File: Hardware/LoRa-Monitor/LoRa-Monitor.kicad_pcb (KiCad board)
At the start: 2 copper layers, 81 parts, among them Q1 ZXTN25100DFH, Q2 ZXTN25100DFH, Q3 ZXTN25100DFH, Q4 ZXTN25100DFH, Q5 ZXTN25100DFH, Q6 ZXTN25100DFH, U1 IRM-05-5, U10 ESP32-S3-WROOM-1, U2 ACPL-M61L, U3 ACPL-M61L, U4 ACPL-M61L, U5 ACPL-M61L, U6 ACPL-M61L, U7 ACPL-M61L, U8 MAX3483, U9 BQ24072RGT

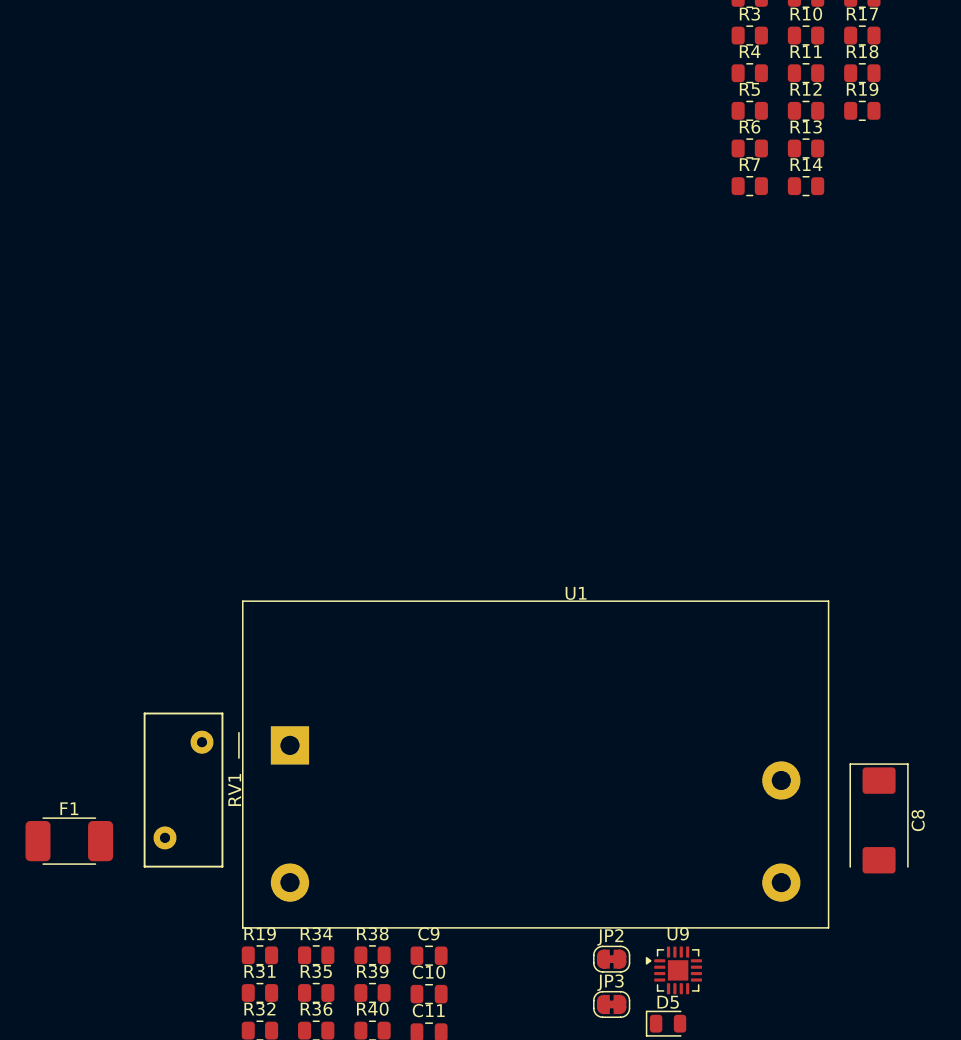
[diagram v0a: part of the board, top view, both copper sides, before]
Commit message: Added more PSU components.
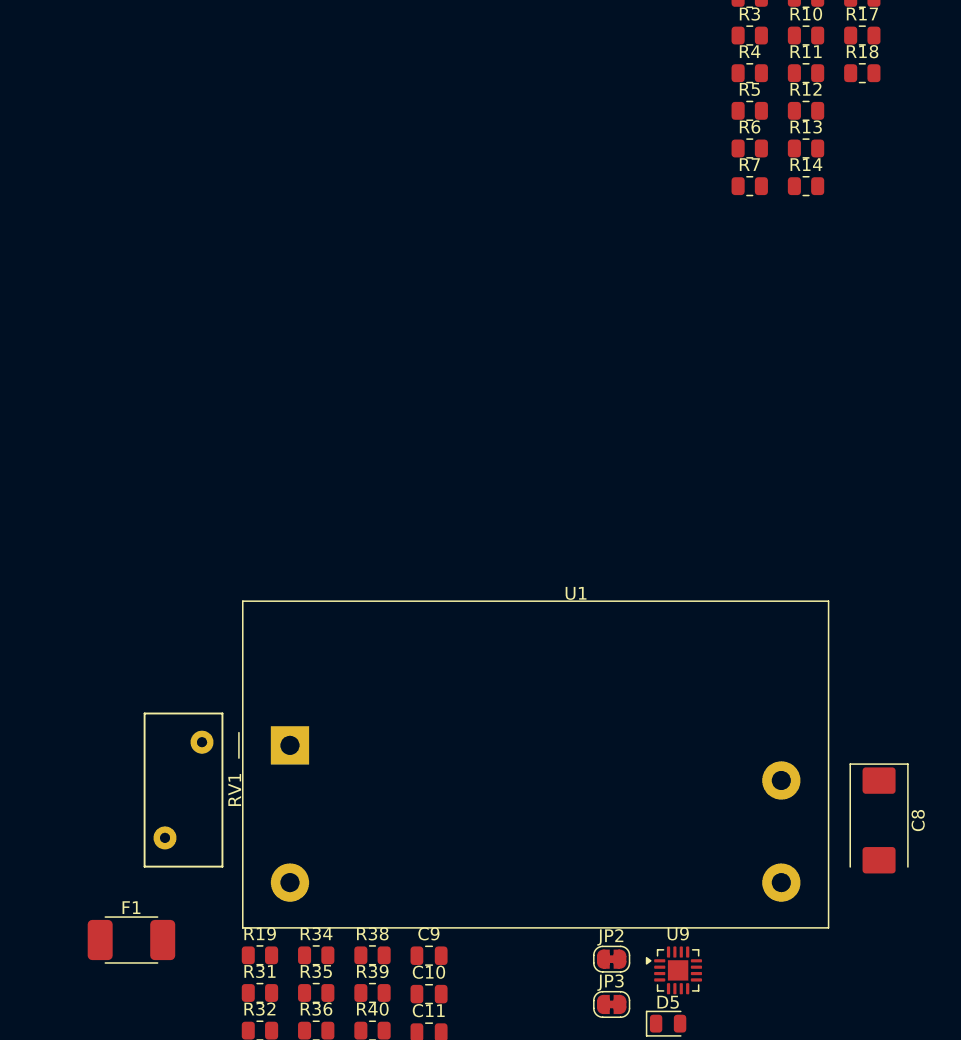
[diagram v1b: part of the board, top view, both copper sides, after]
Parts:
- removed the R19 at (117.7, 78.8)
- U1: footprint Converter_ACDC:Converter_ACDC_MeanWell_IRM-05-xx_THT -> DeviceComponents:Converter_ACDC_MeanWell_IRM-05-xx_THT
- U9: footprint Package_DFN_QFN:VQFN-16-1EP_3x3mm_P0.5mm_EP1.6x1.6mm -> DeviceComponents:VQFN-16-1EP_3x3mm_P0.5mm_EP1.6x1.6mm
- moved F1 9.15 mm to (60.2, 143.8)

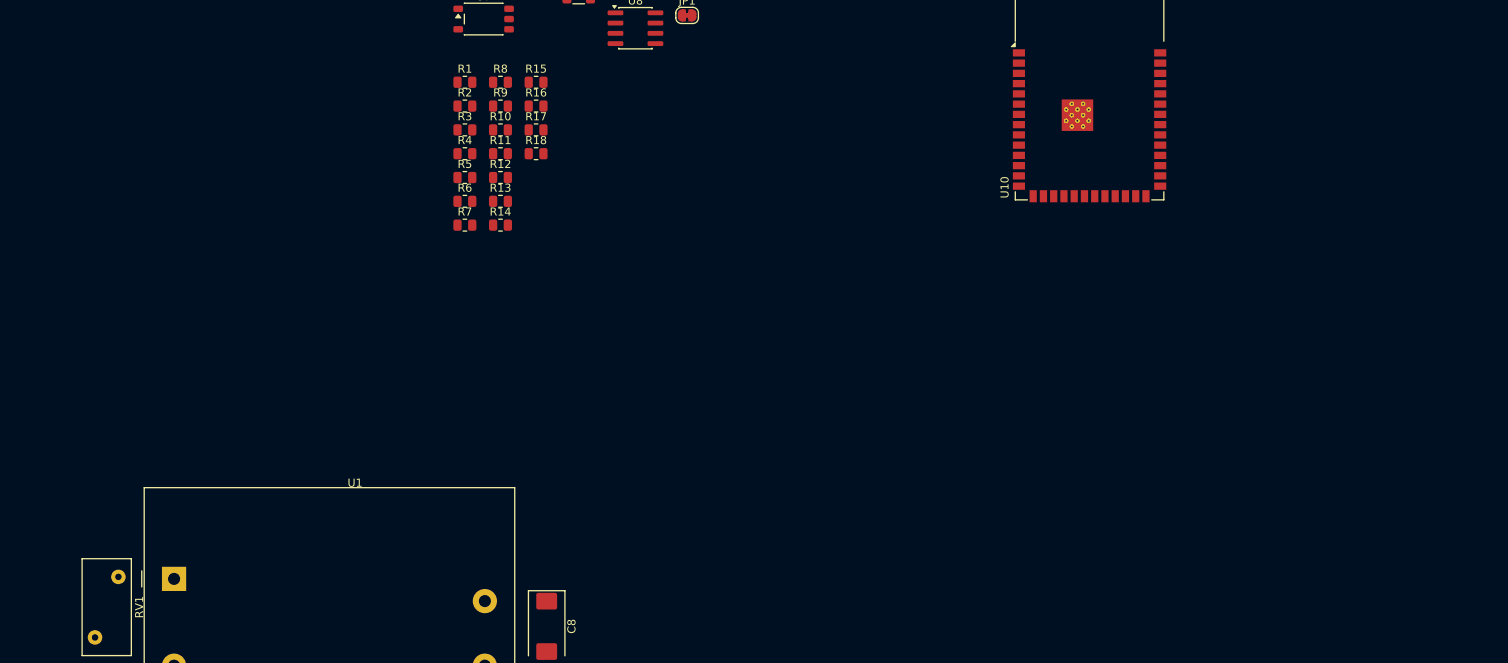
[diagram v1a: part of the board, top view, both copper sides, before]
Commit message: Finished PSU module, started Energy meter
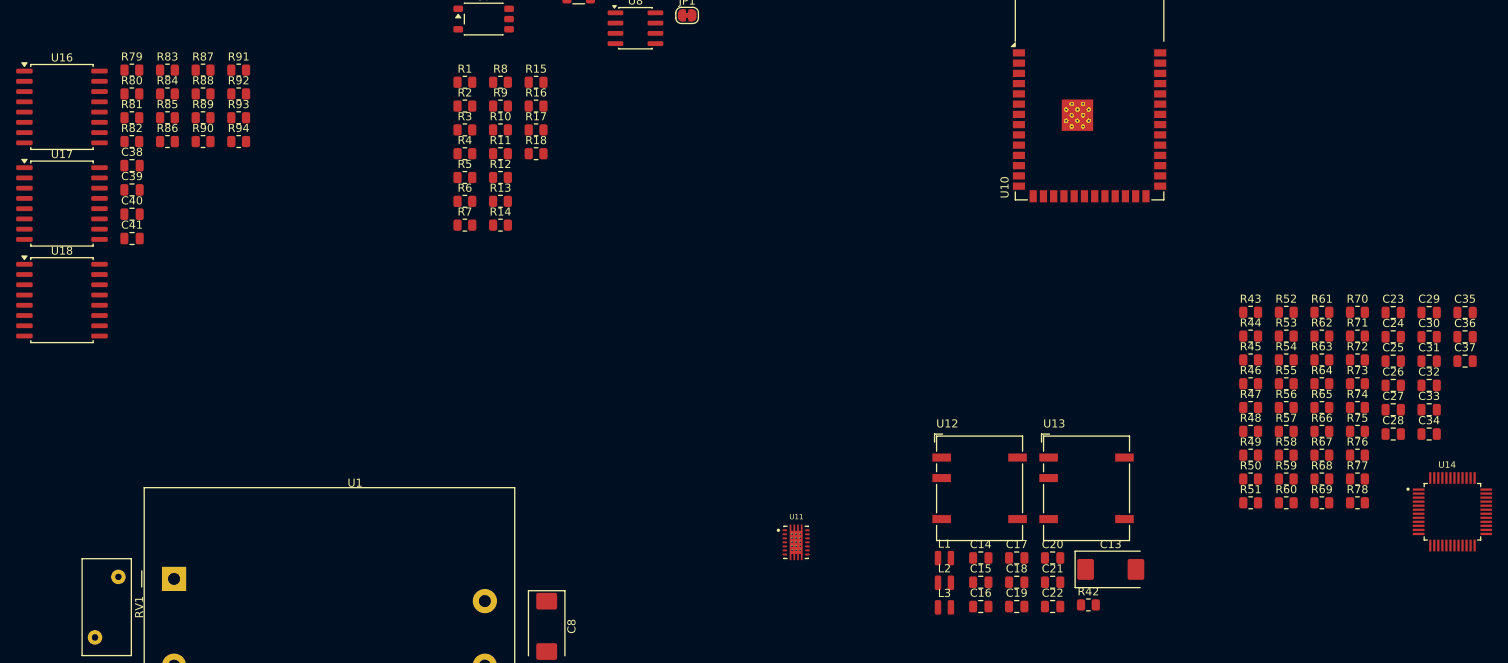
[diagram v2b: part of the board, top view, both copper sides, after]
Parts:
- added C13: 100uF 16V, Capacitor_Tantalum_SMD:CP_EIA-7343-31_Kemet-D, F.Cu at (188.9, 127.3)
- added C14: 10uF, Capacitor_SMD:C_0805_2012Metric, F.Cu at (172.8, 125.9)
- added C15: 10uF, Capacitor_SMD:C_0805_2012Metric, F.Cu at (172.8, 128.9)
- added C16: 22uF, Capacitor_SMD:C_0805_2012Metric, F.Cu at (172.8, 131.9)
- added C17: 100nF, Capacitor_SMD:C_0805_2012Metric, F.Cu at (177.2, 125.9)
- added C18: 1uF, Capacitor_SMD:C_0805_2012Metric, F.Cu at (177.2, 128.9)
- added C19: 22uF, Capacitor_SMD:C_0805_2012Metric, F.Cu at (177.2, 131.9)
- added C20: 22uF, Capacitor_SMD:C_0805_2012Metric, F.Cu at (181.7, 125.9)
- added C21: 100nF, Capacitor_SMD:C_0805_2012Metric, F.Cu at (181.7, 128.9)
- added C22: 1uF, Capacitor_SMD:C_0805_2012Metric, F.Cu at (181.7, 131.9)
- added C23: 4.7uF, Capacitor_SMD:C_0805_2012Metric, F.Cu at (223.9, 95.5)
- added C24: 100nF, Capacitor_SMD:C_0805_2012Metric, F.Cu at (223.9, 98.5)
- added C25: 10uF, Capacitor_SMD:C_0805_2012Metric, F.Cu at (223.9, 101.5)
- added C26: 100nF, Capacitor_SMD:C_0805_2012Metric, F.Cu at (223.9, 104.5)
- added C27: 100nF, Capacitor_SMD:C_0805_2012Metric, F.Cu at (223.9, 107.5)
- added C28: 100nF, Capacitor_SMD:C_0805_2012Metric, F.Cu at (223.9, 110.6)
- added C29: 100nF, Capacitor_SMD:C_0805_2012Metric, F.Cu at (228.3, 95.5)
- added C30: 18nF, Capacitor_SMD:C_0805_2012Metric, F.Cu at (228.3, 98.5)
- added C31: 18nf, Capacitor_SMD:C_0805_2012Metric, F.Cu at (228.3, 101.5)
- added C32: 18nF, Capacitor_SMD:C_0805_2012Metric, F.Cu at (228.3, 104.5)
- added C33: 18nf, Capacitor_SMD:C_0805_2012Metric, F.Cu at (228.3, 107.5)
- added C34: 18nF, Capacitor_SMD:C_0805_2012Metric, F.Cu at (228.3, 110.6)
- added C35: 18nf, Capacitor_SMD:C_0805_2012Metric, F.Cu at (232.8, 95.5)
- added C36: 18nF, Capacitor_SMD:C_0805_2012Metric, F.Cu at (232.8, 98.5)
- added C37: 18nF, Capacitor_SMD:C_0805_2012Metric, F.Cu at (232.8, 101.5)
- added C38: 18nF, Capacitor_SMD:C_0805_2012Metric, F.Cu at (67.6, 77.3)
- added C39: 18nF, Capacitor_SMD:C_0805_2012Metric, F.Cu at (67.6, 80.3)
- added C40: 18nF, Capacitor_SMD:C_0805_2012Metric, F.Cu at (67.6, 83.3)
- added C41: 18nF, Capacitor_SMD:C_0805_2012Metric, F.Cu at (67.6, 86.3)
- added L1: 1uH, DeviceComponents:L_0806_2016Metric, F.Cu at (168.3, 125.9)
- added L2: 15uH, DeviceComponents:L_0806_2016Metric, F.Cu at (168.3, 129.0)
- added L3: 15uH, DeviceComponents:L_0806_2016Metric, F.Cu at (168.3, 132.0)
- added R42: 10k, Resistor_SMD:R_0805_2012Metric, F.Cu at (186.1, 131.7)
- added R43: 10k, Resistor_SMD:R_0805_2012Metric, F.Cu at (206.2, 95.5)
- added R44: 10k, Resistor_SMD:R_0805_2012Metric, F.Cu at (206.2, 98.4)
- added R45: 10k, Resistor_SMD:R_0805_2012Metric, F.Cu at (206.2, 101.4)
- added R46: 10k, Resistor_SMD:R_0805_2012Metric, F.Cu at (206.2, 104.3)
- added R47: 10k, Resistor_SMD:R_0805_2012Metric, F.Cu at (206.2, 107.3)
- added R48: 240k, Resistor_SMD:R_0805_2012Metric, F.Cu at (206.2, 110.2)
- added R49: 240k, Resistor_SMD:R_0805_2012Metric, F.Cu at (206.2, 113.2)
- added R50: 240k, Resistor_SMD:R_0805_2012Metric, F.Cu at (206.2, 116.1)
- added R51: 240k, Resistor_SMD:R_0805_2012Metric, F.Cu at (206.2, 119.1)
- added R52: 240k, Resistor_SMD:R_0805_2012Metric, F.Cu at (210.6, 95.5)
- added R53: 240k, Resistor_SMD:R_0805_2012Metric, F.Cu at (210.6, 98.4)
- added R54: 240k, Resistor_SMD:R_0805_2012Metric, F.Cu at (210.6, 101.4)
- added R55: 1k, Resistor_SMD:R_0805_2012Metric, F.Cu at (210.6, 104.3)
- added R56: 1k, Resistor_SMD:R_0805_2012Metric, F.Cu at (210.6, 107.3)
- added R57: 240k, Resistor_SMD:R_0805_2012Metric, F.Cu at (210.6, 110.2)
- added R58: 240k, Resistor_SMD:R_0805_2012Metric, F.Cu at (210.6, 113.2)
- added R59: 240k, Resistor_SMD:R_0805_2012Metric, F.Cu at (210.6, 116.1)
- added R60: 240k, Resistor_SMD:R_0805_2012Metric, F.Cu at (210.6, 119.1)
- added R61: 240k, Resistor_SMD:R_0805_2012Metric, F.Cu at (215.0, 95.5)
- added R62: 240k, Resistor_SMD:R_0805_2012Metric, F.Cu at (215.0, 98.4)
- added R63: 240k, Resistor_SMD:R_0805_2012Metric, F.Cu at (215.0, 101.4)
- added R64: 1k, Resistor_SMD:R_0805_2012Metric, F.Cu at (215.0, 104.3)
- added R65: 1k, Resistor_SMD:R_0805_2012Metric, F.Cu at (215.0, 107.3)
- added R66: 240k, Resistor_SMD:R_0805_2012Metric, F.Cu at (215.0, 110.2)
- added R67: 240k, Resistor_SMD:R_0805_2012Metric, F.Cu at (215.0, 113.2)
- added R68: 240k, Resistor_SMD:R_0805_2012Metric, F.Cu at (215.0, 116.1)
- added R69: 240k, Resistor_SMD:R_0805_2012Metric, F.Cu at (215.0, 119.1)
- added R70: 240k, Resistor_SMD:R_0805_2012Metric, F.Cu at (219.4, 95.5)
- added R71: 240k, Resistor_SMD:R_0805_2012Metric, F.Cu at (219.4, 98.4)
- added R72: 240k, Resistor_SMD:R_0805_2012Metric, F.Cu at (219.4, 101.4)
- added R73: 1k, Resistor_SMD:R_0805_2012Metric, F.Cu at (219.4, 104.3)
- added R74: 1k, Resistor_SMD:R_0805_2012Metric, F.Cu at (219.4, 107.3)
- added R75: 2.4R, Resistor_SMD:R_0805_2012Metric, F.Cu at (219.4, 110.2)
- added R76: 2.4R, Resistor_SMD:R_0805_2012Metric, F.Cu at (219.4, 113.2)
- added R77: 1k, Resistor_SMD:R_0805_2012Metric, F.Cu at (219.4, 116.1)
- added R78: 1k, Resistor_SMD:R_0805_2012Metric, F.Cu at (219.4, 119.1)
- added R79: 2.4R, Resistor_SMD:R_0805_2012Metric, F.Cu at (67.6, 65.5)
- added R80: 2.4R, Resistor_SMD:R_0805_2012Metric, F.Cu at (67.6, 68.4)
- added R81: 1k, Resistor_SMD:R_0805_2012Metric, F.Cu at (67.6, 71.4)
- added R82: 1k, Resistor_SMD:R_0805_2012Metric, F.Cu at (67.6, 74.3)
- added R83: 2.4R, Resistor_SMD:R_0805_2012Metric, F.Cu at (72.0, 65.5)
- added R84: 2.4R, Resistor_SMD:R_0805_2012Metric, F.Cu at (72.0, 68.4)
- added R85: 1k, Resistor_SMD:R_0805_2012Metric, F.Cu at (72.0, 71.4)
- added R86: 1k, Resistor_SMD:R_0805_2012Metric, F.Cu at (72.0, 74.3)
- added R87: 10k, Resistor_SMD:R_0805_2012Metric, F.Cu at (76.4, 65.5)
- added R88: 10k, Resistor_SMD:R_0805_2012Metric, F.Cu at (76.4, 68.4)
- added R89: 10k, Resistor_SMD:R_0805_2012Metric, F.Cu at (76.4, 71.4)
- added R90: 10k, Resistor_SMD:R_0805_2012Metric, F.Cu at (76.4, 74.3)
- added R91: 10k, Resistor_SMD:R_0805_2012Metric, F.Cu at (80.8, 65.5)
- added R92: 10k, Resistor_SMD:R_0805_2012Metric, F.Cu at (80.8, 68.4)
- added R93: 10k, Resistor_SMD:R_0805_2012Metric, F.Cu at (80.8, 71.4)
- added R94: 10k, Resistor_SMD:R_0805_2012Metric, F.Cu at (80.8, 74.3)
- added U11: TPS63021DSJR, DeviceComponents:IC_TPS63021DSJR, F.Cu at (149.9, 124.0)
- added U12: NXE1S0303MC, Converter_DCDC:Converter_DCDC_Murata_NXExSxxxxMC_SMD, F.Cu at (172.6, 118.5)
- added U13: NXE1S0303MC, Converter_DCDC:Converter_DCDC_Murata_NXExSxxxxMC_SMD, F.Cu at (185.9, 118.5)
- added U14: ATM90E32AS-AU-R, DeviceComponents:QFP50P900X900X120-48N, F.Cu at (231.2, 120.2)
- added U16: ADuM1401xRW, Package_SO:SOIC-16W_7.5x10.3mm_P1.27mm, F.Cu at (59.0, 70.0)
- added U17: ADuM1401xRW, Package_SO:SOIC-16W_7.5x10.3mm_P1.27mm, F.Cu at (59.0, 82.0)
- added U18: ADuM1401xRW, Package_SO:SOIC-16W_7.5x10.3mm_P1.27mm, F.Cu at (59.0, 94.0)

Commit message: Finished schematic, started with PCB design
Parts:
- added C42: 100nF, Capacitor_SMD:C_0805_2012Metric, F.Cu at (282.9, 111.8)
- added C43: 100nF, Capacitor_SMD:C_0805_2012Metric, F.Cu at (378.7, 48.1)
- added C44: 10uF, Capacitor_SMD:C_0805_2012Metric, F.Cu at (378.7, 51.1)
- added C45: 100nF, Capacitor_SMD:C_0805_2012Metric, F.Cu at (351.1, 77.1)
- added C46: 10uF, Capacitor_SMD:C_0805_2012Metric, F.Cu at (263.1, -52.1)
- added C47: 100nF, Capacitor_SMD:C_0805_2012Metric, F.Cu at (265.3, -52.1)
- added C48: 10uF, Capacitor_SMD:C_0805_2012Metric, F.Cu at (282.9, 114.8)
- added C49: 100nF, Capacitor_SMD:C_0805_2012Metric, F.Cu at (282.9, 117.8)
- added C50: 10uF, Capacitor_SMD:C_0805_2012Metric, F.Cu at (282.9, 120.8)
- added C51: 10uF, Capacitor_SMD:C_0805_2012Metric, F.Cu at (282.9, 123.8)
- added D6: SK6812MINI-012, DeviceComponents:LED_SK6812MINI-012, F.Cu at (350.1, 81.8)
- added J1: USB_C_Receptacle_USB2.0_16P, Connector_USB:USB_C_Receptacle_HRO_TYPE-C-31-M-12, F.Cu at (247.1, -49.6)
- added J10: AudioJack3, Connector_Audio:Jack_3.5mm_CUI_SJ1-3523N_Horizontal, F.Cu at (300.4, 71.5)
- added J11: Screw_Terminal_01x02, TerminalBlock_Phoenix:TerminalBlock_Phoenix_PT-1,5-2-5.0-H_1x02_P5.00mm_Horizontal, F.Cu at (256.5, 90.7)
- added J12: Screw_Terminal_01x02, TerminalBlock_Phoenix:TerminalBlock_Phoenix_PT-1,5-2-5.0-H_1x02_P5.00mm_Horizontal, F.Cu at (256.5, 102.0)
- added J13: Conn_01x02_Pin, Connector_JST:JST_PH_B2B-PH-K_1x02_P2.00mm_Vertical, F.Cu at (299.5, 81.3)
- added J14: Conn_01x02_Pin, Connector_JST:JST_PH_B2B-PH-K_1x02_P2.00mm_Vertical, F.Cu at (299.0, 96.2)
- added J2: Micro_SD_Card, Connector_Card:microSD_HC_Molex_47219-2001, F.Cu at (368.1, 54.6)
- added J3: Conn_02x03_Odd_Even, Connector_PinHeader_2.54mm:PinHeader_2x03_P2.54mm_Vertical, F.Cu at (279.0, 92.2)
- added J4: Conn_Coaxial, Connector_Coaxial:SMA_Amphenol_901-144_Vertical, F.Cu at (291.8, 83.2)
- added J5: Screw_Terminal_01x02, TerminalBlock_Phoenix:TerminalBlock_Phoenix_PT-1,5-2-5.0-H_1x02_P5.00mm_Horizontal, F.Cu at (256.5, 68.0)
- added J6: Screw_Terminal_01x02, TerminalBlock_Phoenix:TerminalBlock_Phoenix_PT-1,5-2-5.0-H_1x02_P5.00mm_Horizontal, F.Cu at (256.5, 79.3)
- added J7: AudioJack3, Connector_Audio:Jack_3.5mm_CUI_SJ1-3523N_Horizontal, F.Cu at (272.1, 71.5)
- added J8: AudioJack3, Connector_Audio:Jack_3.5mm_CUI_SJ1-3523N_Horizontal, F.Cu at (286.2, 71.5)
- added J9: Screw_Terminal_01x04, TerminalBlock_Phoenix:TerminalBlock_Phoenix_PT-1,5-4-5.0-H_1x04_P5.00mm_Horizontal, F.Cu at (268.6, 83.6)
- added R0: 0R, Resistor_SMD:R_0603_1608Metric, F.Cu at (287.7, -35.8)
- added R100: 10k, Resistor_SMD:R_0805_2012Metric, F.Cu at (282.9, 135.6)
- added R101: 10k, Resistor_SMD:R_0805_2012Metric, F.Cu at (258.3, -49.8)
- added R102: 10k, Resistor_SMD:R_1206_3216Metric, F.Cu at (319.5, 88.1)
- added R103: 46.4k, Resistor_SMD:R_0805_2012Metric, F.Cu at (311.6, 64.5)
- added R104: 10k, Resistor_SMD:R_0805_2012Metric, F.Cu at (311.6, 67.4)
- added R105: 1.1k, Resistor_SMD:R_0805_2012Metric, F.Cu at (311.6, 70.4)
- added R106: 140k, Resistor_SMD:R_0805_2012Metric, F.Cu at (311.6, 73.3)
- added R107: 10k, Resistor_SMD:R_0805_2012Metric, F.Cu at (311.6, 76.3)
- added R108: 1.1k, Resistor_SMD:R_0805_2012Metric, F.Cu at (311.6, 79.2)
- added R109: 1.1k, Resistor_SMD:R_0805_2012Metric, F.Cu at (311.6, 82.2)
- added R110: 10k, Resistor_SMD:R_0805_2012Metric, F.Cu at (311.6, 85.1)
- added R111: 10k, Resistor_SMD:R_0805_2012Metric, F.Cu at (609.9, 225.1)
- added R112: 10k, Resistor_SMD:R_0805_2012Metric, F.Cu at (609.9, 228.1)
- added R113: 10k, Resistor_SMD:R_0805_2012Metric, F.Cu at (609.9, 231.0)
- added R114: 240k, Resistor_SMD:R_0805_2012Metric, F.Cu at (571.6, 205.9)
- added R115: 10k, Resistor_SMD:R_0805_2012Metric, F.Cu at (225.5, 143.0)
- added R95: 10k, Resistor_SMD:R_0805_2012Metric, F.Cu at (282.9, 126.8)
- added R96: 10k, Resistor_SMD:R_0805_2012Metric, F.Cu at (357.5, 51.0)
- added R97: 10k, Resistor_SMD:R_0805_2012Metric, F.Cu at (289.4, 117.6)
- added R98: 10k, Resistor_SMD:R_0805_2012Metric, F.Cu at (282.9, 129.7)
- added R99: 10k, Resistor_SMD:R_0805_2012Metric, F.Cu at (282.9, 132.7)
- added RRX1: 0R, Resistor_SMD:R_0603_1608Metric, F.Cu at (287.7, -48.5)
- added RTX1: 0R, Resistor_SMD:R_0603_1608Metric, F.Cu at (290.8, -47.2)
- added U15: E22-900M30S, DeviceComponents:XCVR_E22-900M30S, F.Cu at (266.4, 130.3)
- C23: value 4.7uF -> 10uF
- R1, R10, R11, R12, R13, R14, R15, R16, R17, R2, R3, R4, R5, R6, R7, R8, R9: footprint Resistor_SMD:R_0805_2012Metric -> Resistor_SMD:R_0603_1608Metric
- R18: value R -> 0R; footprint Resistor_SMD:R_0805_2012Metric -> Resistor_SMD:R_0603_1608Metric
- R21: value 10k -> 0R; footprint Resistor_SMD:R_1206_3216Metric -> Resistor_SMD:R_0603_1608Metric
- R35: value 46.4k -> 0R; footprint Resistor_SMD:R_0805_2012Metric -> Resistor_SMD:R_0603_1608Metric
- R36, R37, R42, R45, R46, R47: value 10k -> 0R; footprint Resistor_SMD:R_0805_2012Metric -> Resistor_SMD:R_0603_1608Metric
- R38, R40, R41: value 1.1k -> 0R; footprint Resistor_SMD:R_0805_2012Metric -> Resistor_SMD:R_0603_1608Metric
- R39: value 140k -> 0R; footprint Resistor_SMD:R_0805_2012Metric -> Resistor_SMD:R_0603_1608Metric
- R48: value 240k -> 0R; footprint Resistor_SMD:R_0805_2012Metric -> Resistor_SMD:R_0603_1608Metric
- U2, U3, U4, U5, U6, U7: footprint Package_SO:SO-5-6_4.55x3.7mm_P1.27mm -> DeviceComponents:SO-5_4.39x3.84mm_P1.27mm
- moved R87 544.8 mm to (593.0, 238.5)
- moved R88 544.8 mm to (593.0, 241.4)
- moved C40 540.0 mm to (568.1, 286.2), turned to 90 degrees
- moved R85 538.4 mm to (565.3, 287.1), turned to 180 degrees
- moved R83 537.9 mm to (562.5, 286.3), turned to 90 degrees
- moved C41 537.6 mm to (568.1, 282.6), turned to 90 degrees
- moved R84 535.2 mm to (562.5, 282.6), turned to 90 degrees
- moved R86 535.1 mm to (565.3, 281.7), turned to 180 degrees
- moved C38 525.3 mm to (560.6, 258.7), turned to 90 degrees
- moved R81 525.1 mm to (557.8, 259.6), turned to 180 degrees
- moved R79 524.3 mm to (555.0, 258.7), turned to 90 degrees
- moved C39 523.0 mm to (560.6, 255.1), turned to 90 degrees
- moved R82 522.1 mm to (557.8, 254.3)
- moved R80 521.9 mm to (555.0, 255.1), turned to 90 degrees
- moved R61 425.6 mm to (625.5, 207.9)
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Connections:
- net /Energy Meter Interface Module/485_A renamed /Connectors/485_A
- net /Energy Meter Interface Module/485_B renamed /Connectors/485_B
- net /Energy Meter Interface Module/PULSE_IN1+ renamed /Connectors/PULSE_IN1+
- net /Energy Meter Interface Module/PULSE_IN1- renamed /Connectors/PULSE_IN1-
- net /Energy Meter Interface Module/PULSE_IN2- renamed /Connectors/PULSE_IN2-
- net /Energy Meter Interface Module/PULSE_IN3+ renamed /Connectors/PULSE_IN3+
- net /Energy Meter Interface Module/PULSE_IN3- renamed /Connectors/PULSE_IN3-
- net /Energy meter/IA+ renamed /Connectors/IA+
- net /Energy meter/IA- renamed /Connectors/IA-
- net /Energy meter/IB+ renamed /Connectors/IB+
- net /Energy meter/IB- renamed /Connectors/IB-
- net /Energy meter/IC+ renamed /Connectors/IC+
- net /Energy meter/IC- renamed /Connectors/IC-
- net VBAT renamed /Connectors/BATT+
- C12 pad 1: VCC -> VBUS
- C13 pad 1: VCC -> VBUS
- C15 pad 1: +3.3V_485 -> GND_M90
- C15 pad 2: GND_485 -> +3.3V_M90
- C16 pad 1: VCC -> VBUS
- C17 pad 1: VCC -> VBUS
- C23 pad 2: GND_485 -> GND_M90
- C24 pad 2: GND_485 -> GND_M90
- C25 pad 2: GND_485 -> GND_M90
- C26 pad 2: GND_485 -> GND_M90
- C27 pad 2: GND_485 -> GND_M90
- C28 pad 1: +3.3V_485 -> +3.3V_M90
- C28 pad 2: GND_485 -> GND_M90
- C29 pad 1: +3.3V_485 -> +3.3V_M90
- C29 pad 2: GND_485 -> GND_M90
- C30 pad 2: GND_485 -> GND_M90
- C31 pad 2: GND_485 -> GND_M90
- C32 pad 2: GND_485 -> GND_M90
- C33 pad 2: GND_485 -> GND_M90
- C34 pad 2: GND_485 -> GND_M90
- C35 pad 2: GND_485 -> GND_M90
- C36 pad 2: GND_485 -> GND_M90
- C37 pad 1: GND_485 -> GND_M90
- C38 pad 2: GND_485 -> GND_M90
- C39 pad 1: GND_485 -> GND_M90
- C40 pad 2: GND_485 -> GND_M90
- C41 pad 1: GND_485 -> GND_M90
- D2 pad 2: /Energy Meter Interface Module/PULSE_IN2+ -> /Connectors/PULSE_IN2+
- D5 pad 2: VCC -> VBUS
- F1 pad 1: /Power supply/AC_L -> /Connectors/Ua
- L3 pad 2: +3.3V_485 -> GND_M90
- R1 pad 1: unconnected-(R1-Pad1) -> /Energy meter/IRQ0
- R1 pad 2: Net-(U10-IO0) -> Net-(U10-IO1)
- R10 pad 1: unconnected-(R10-Pad1) -> /Energy Meter Interface Module/PULSE_IN2_3V3
- R10 pad 2: Net-(U10-IO9) -> Net-(U10-IO10)
- R11 pad 1: unconnected-(R11-Pad1) -> /Energy Meter Interface Module/PULSE_IN3_3V3
- R11 pad 2: Net-(U10-IO10) -> Net-(U10-IO11)
- R12 pad 1: unconnected-(R12-Pad1) -> /LoRa Module/~{RST_E22}
- R12 pad 2: Net-(U10-IO11) -> Net-(U10-IO12)
- R13 pad 1: unconnected-(R13-Pad1) -> /Energy meter/CS_ATM90
- R13 pad 2: Net-(U10-IO12) -> Net-(U10-IO13)
- R14 pad 1: unconnected-(R14-Pad1) -> /Energy meter/SCKL_SPI0
- R14 pad 2: Net-(U10-IO13) -> Net-(U10-IO14)
- R15 pad 1: unconnected-(R15-Pad1) -> /Energy meter/SDI_SPI0
- R15 pad 2: Net-(U10-IO14) -> Net-(U10-IO15)
- R16 pad 1: unconnected-(R16-Pad1) -> /Energy meter/SDO_SPI0
- R16 pad 2: Net-(U10-IO15) -> Net-(U10-IO16)
- R17 pad 1: unconnected-(R17-Pad1) -> Net-(U10-IO17)
- R17 pad 2: Net-(U10-IO16) -> /Energy Meter Interface Module/RXD_485
- R18 pad 1: Net-(U10-EN) -> Net-(U10-IO18)
- R18 pad 2: +3.3V -> /Energy Meter Interface Module/TXD_485
- R2 pad 1: unconnected-(R2-Pad1) -> /Energy meter/IRQ1
- R2 pad 2: Net-(U10-IO1) -> Net-(U10-IO2)
- R21 pad 1: /Energy Meter Interface Module/PULSE_IN2+ -> Net-(U10-IO21)
- R21 pad 2: Net-(Q2-C) -> /Energy Meter Interface Module/EN_485
- R3 pad 1: unconnected-(R3-Pad1) -> /Energy meter/WARNOUT
- R3 pad 2: Net-(U10-IO2) -> Net-(U10-IO3)
- R35 pad 1: GND -> Net-(U10-IO35)
- R35 pad 2: Net-(U9-TMR) -> /LoRa Module/BUSY_E22
- R36 pad 1: Net-(JP2-A) -> Net-(U10-IO36)
- R36 pad 2: GND -> /LoRa Module/DIO1_E22
- R37 pad 1: Net-(U9-EN2) -> Net-(U10-IO37)
- R37 pad 2: +5V -> /LoRa Module/DIO2_E22
- R38 pad 1: Net-(JP3-A) -> Net-(U10-IO38)
- R38 pad 2: GND -> /MCU/SDO_SPI1
- R39 pad 1: Net-(JP3-A) -> Net-(U10-IO39)
- R39 pad 2: /Power supply/THERM_BATT+ -> /MCU/SDI_SPI1
- R4 pad 1: unconnected-(R4-Pad1) -> /Energy meter/PM0
- R4 pad 2: Net-(U10-IO3) -> Net-(U10-IO4)
- R40 pad 1: Net-(U9-~{PGOOD}) -> Net-(U10-IO40)
- R40 pad 2: Net-(D5-K) -> /MCU/SCLK_SPI1
- R41 pad 1: Net-(U9-~{CHG}) -> Net-(U10-IO41)
- R41 pad 2: +3.3V -> /LoRa Module/CS_E22
- R42 pad 1: Net-(U11-EN) -> Net-(U10-IO42)
- R42 pad 2: VCC -> /MCU/CS_SD
- R43 pad 2: +3.3V_485 -> +3.3V_M90
- R44 pad 1: +3.3V_485 -> +3.3V_M90
- R45 pad 1: +3.3V_485 -> Net-(U10-IO45)
- R45 pad 2: /Energy meter/SCKL -> /MCU/LED_CTRL
- R46 pad 1: +3.3V_485 -> Net-(U10-IO46)
- R46 pad 2: /Energy meter/SDI -> Net-(R46-Pad2)
- R47 pad 1: +3.3V_485 -> Net-(U10-IO47)
- R47 pad 2: /Energy meter/SDO -> /LoRa Module/RXEN_E22
- R48 pad 1: Net-(R48-Pad1) -> Net-(U10-IO48)
- R48 pad 2: /Energy meter/Ua -> /LoRa Module/TXEN_E22
- R49 pad 2: Net-(R48-Pad1) -> Net-(R114-Pad1)
- R5 pad 1: unconnected-(R5-Pad1) -> /Energy meter/PM1
- R5 pad 2: Net-(U10-IO4) -> Net-(U10-IO5)
- R55 pad 2: GND_485 -> GND_M90
- R56 pad 2: GND_485 -> GND_M90
- R57 pad 2: /Energy meter/Ub -> /Connectors/Ub
- R6 pad 1: unconnected-(R6-Pad1) -> /Energy meter/ZX0
- R6 pad 2: Net-(U10-IO5) -> Net-(U10-IO6)
- R64 pad 2: GND_485 -> GND_M90
- R65 pad 2: GND_485 -> GND_M90
- R66 pad 2: /Energy meter/Uc -> /Connectors/Uc
- R7 pad 1: unconnected-(R7-Pad1) -> /Energy meter/ZX1
- R7 pad 2: Net-(U10-IO6) -> Net-(U10-IO7)
- R73 pad 2: GND_485 -> GND_M90
- R74 pad 2: GND_485 -> GND_M90
- R75 pad 2: GND_485 -> GND_M90
- R76 pad 1: GND_485 -> GND_M90
- R79 pad 2: GND_485 -> GND_M90
- R8 pad 1: unconnected-(R8-Pad1) -> /Energy meter/ZX2
- R8 pad 2: Net-(U10-IO7) -> Net-(U10-IO8)
- R80 pad 1: GND_485 -> GND_M90
- R83 pad 2: GND_485 -> GND_M90
- R84 pad 1: GND_485 -> GND_M90
- R87 pad 1: +3.3V_485 -> +3.3V_M90
- R87 pad 2: /Energy meter/PM1 -> /Energy meter/PM1_M90
- R88 pad 1: +3.3V_485 -> +3.3V_M90
- R88 pad 2: /Energy meter/PM0 -> /Energy meter/PM0_M90
- R89 pad 1: +3.3V_485 -> +3.3V_M90
- R9 pad 1: unconnected-(R9-Pad1) -> /Energy Meter Interface Module/PULSE_IN1_3V3
- R9 pad 2: Net-(U10-IO8) -> Net-(U10-IO9)
- R90 pad 1: unconnected-(R90-Pad1) -> Net-(U16-VE1)
- R93 pad 1: +3.3V_485 -> +3.3V_M90
- R94 pad 1: +3.3V_485 -> +3.3V_M90
- RV1 pad 2: /Power supply/AC_N -> GND_M90
- U1 pad 1: /Power supply/AC_N -> GND_M90
- U10 pad 10: unconnected-(U10-IO17-Pad10) -> Net-(U10-IO17)
- U10 pad 11: unconnected-(U10-IO18-Pad11) -> Net-(U10-IO18)
- U10 pad 13: unconnected-(U10-USB_D--Pad13) -> /Connectors/USB_D-
- U10 pad 14: unconnected-(U10-USB_D+-Pad14) -> /Connectors/USB_D+
- U10 pad 16: unconnected-(U10-IO46-Pad16) -> Net-(U10-IO46)
- U10 pad 23: unconnected-(U10-IO21-Pad23) -> Net-(U10-IO21)
- U10 pad 24: unconnected-(U10-IO47-Pad24) -> Net-(U10-IO47)
- U10 pad 25: unconnected-(U10-IO48-Pad25) -> Net-(U10-IO48)
- U10 pad 26: unconnected-(U10-IO45-Pad26) -> Net-(U10-IO45)
- U10 pad 28: unconnected-(U10-IO35-Pad28) -> Net-(U10-IO35)
- U10 pad 29: unconnected-(U10-IO36-Pad29) -> Net-(U10-IO36)
- U10 pad 3: Net-(U10-EN) -> /Connectors/ESP_EN
- U10 pad 30: unconnected-(U10-IO37-Pad30) -> Net-(U10-IO37)
- U10 pad 31: unconnected-(U10-IO38-Pad31) -> Net-(U10-IO38)
- U10 pad 32: unconnected-(U10-IO39-Pad32) -> Net-(U10-IO39)
- U10 pad 33: unconnected-(U10-IO40-Pad33) -> Net-(U10-IO40)
- U10 pad 34: unconnected-(U10-IO41-Pad34) -> Net-(U10-IO41)
- U10 pad 35: unconnected-(U10-IO42-Pad35) -> Net-(U10-IO42)
- U10 pad 36: unconnected-(U10-RXD0-Pad36) -> Net-(U10-RXD0)
- U10 pad 37: unconnected-(U10-TXD0-Pad37) -> Net-(U10-TXD0)
- U11 pad 10: VCC -> VBUS
- U11 pad 11: VCC -> VBUS
- U11 pad 16: (no net) -> GND
- U11 pad 17: (no net) -> GND
- U11 pad 18: (no net) -> GND
- U11 pad 19: (no net) -> GND
- U11 pad 20: (no net) -> GND
- U11 pad 21: (no net) -> GND
- U11 pad 22: (no net) -> GND
- U11 pad 23: (no net) -> GND
- U11 pad 24: (no net) -> GND
- U11 pad 25: (no net) -> GND
- U11 pad 26: (no net) -> GND
- U11 pad 27: (no net) -> GND
- U11 pad 28: (no net) -> GND
- U11 pad 29: (no net) -> GND
- U11 pad 30: (no net) -> GND
- U13 pad 7: GND_485 -> +3.3V_M90
- U14 pad 1: +3.3V_485 -> +3.3V_M90
- U14 pad 10: GND_485 -> GND_M90
- U14 pad 12: GND_485 -> GND_M90
- U14 pad 19: GND_485 -> GND_M90
- U14 pad 2: GND_485 -> GND_M90
- U14 pad 22: /Energy meter/ZX0 -> /Energy meter/ZX0_M90
- U14 pad 23: /Energy meter/ZX1 -> /Energy meter/ZX1_M90
- U14 pad 24: /Energy meter/ZX2 -> /Energy meter/ZX2_M90
- U14 pad 29: /Energy meter/WARNOUT -> /Energy meter/WARNOUT_M90
- U14 pad 30: /Energy meter/IRQ0 -> /Energy meter/IRQ0_M90
- U14 pad 31: /Energy meter/IRQ1 -> /Energy meter/IRQ1_M90
- U14 pad 32: GND_485 -> GND_M90
- U14 pad 33: /Energy meter/PM0 -> /Energy meter/PM0_M90
- U14 pad 34: /Energy meter/PM1 -> /Energy meter/PM1_M90
- U14 pad 35: (no net) -> unconnected-(U14-NC-Pad35)
- U14 pad 36: GND_485 -> GND_M90
- U14 pad 44: GND_485 -> GND_M90
- U14 pad 45: (no net) -> unconnected-(U14-NC-Pad45)
- U14 pad 46: (no net) -> unconnected-(U14-NC-Pad46)
- U14 pad 47: GND_485 -> GND_M90
- U14 pad 48: +3.3V_485 -> +3.3V_M90
- U14 pad 9: GND_485 -> GND_M90
- U16 pad 15: GND_485 -> GND_M90
- U16 pad 16: +3.3V_485 -> +3.3V_M90
- U16 pad 3: unconnected-(U16-VIA-Pad3) -> /Energy meter/CS_ATM90
- U16 pad 4: unconnected-(U16-VIB-Pad4) -> /Energy meter/SCKL_SPI0
- U16 pad 5: unconnected-(U16-VIC-Pad5) -> /Energy meter/SDI_SPI0
- U16 pad 6: unconnected-(U16-VOD-Pad6) -> /Energy meter/SDO_SPI0
- U16 pad 7: unconnected-(U16-VE1-Pad7) -> Net-(U16-VE1)
- U16 pad 9: GND_485 -> GND_M90
- U17 pad 1: +3.3V_485 -> +3.3V_M90
- U17 pad 11: unconnected-(U17-VID-Pad11) -> /Energy meter/PM0
- U17 pad 12: unconnected-(U17-VOC-Pad12) -> /Energy meter/ZX2
- U17 pad 13: unconnected-(U17-VOB-Pad13) -> /Energy meter/ZX1
- U17 pad 14: unconnected-(U17-VOA-Pad14) -> /Energy meter/ZX0
- U17 pad 2: GND_485 -> GND_M90
- U17 pad 3: /Energy meter/ZX0 -> /Energy meter/ZX0_M90
- U17 pad 4: /Energy meter/ZX1 -> /Energy meter/ZX1_M90
- U17 pad 5: /Energy meter/ZX2 -> /Energy meter/ZX2_M90
- U17 pad 6: /Energy meter/PM0 -> /Energy meter/PM0_M90
- U17 pad 8: GND_485 -> GND_M90
- U18 pad 1: +3.3V_485 -> +3.3V_M90
- U18 pad 11: unconnected-(U18-VID-Pad11) -> /Energy meter/PM1
- U18 pad 12: unconnected-(U18-VOC-Pad12) -> /Energy meter/WARNOUT
- U18 pad 13: unconnected-(U18-VOB-Pad13) -> /Energy meter/IRQ1
- U18 pad 14: unconnected-(U18-VOA-Pad14) -> /Energy meter/IRQ0
- U18 pad 2: GND_485 -> GND_M90
- U18 pad 3: /Energy meter/IRQ0 -> /Energy meter/IRQ0_M90
- U18 pad 4: /Energy meter/IRQ1 -> /Energy meter/IRQ1_M90
- U18 pad 5: /Energy meter/WARNOUT -> /Energy meter/WARNOUT_M90
- U18 pad 6: /Energy meter/PM1 -> /Energy meter/PM1_M90
- U18 pad 8: GND_485 -> GND_M90
- U3 pad 1: /Energy Meter Interface Module/PULSE_IN2+ -> /Connectors/PULSE_IN2+
- U9 pad 10: VCC -> VBUS
- U9 pad 11: VCC -> VBUS
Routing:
- net /Connectors/USB_D+: track 0.00 -> 27.5 mm
- net /Connectors/USB_D-: track 0.00 -> 26.7 mm
- net (no net): track 0.00 -> 14.9 mm
- net Net-(U10-IO16): track 0.00 -> 5.12 mm
- net Net-(U10-IO7): track 0.00 -> 5.12 mm
- net Net-(U10-IO15): track 0.00 -> 2.07 mm
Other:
- board outline added: 13 x 1.4 mm

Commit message: Started routing.
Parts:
- moved R57 576.1 mm to (56.8, 98.9), turned to 180 degrees
- moved R58 574.5 mm to (58.6, 101.0), turned to 180 degrees
- moved R59 573.7 mm to (60.4, 98.9), turned to 180 degrees
- moved R60 572.1 mm to (62.3, 101.0), turned to 180 degrees
- moved R61 571.9 mm to (64.1, 98.9), turned to 180 degrees
- moved R62 570.3 mm to (65.9, 101.0), turned to 180 degrees
- moved R63 569.5 mm to (67.7, 98.9), turned to 180 degrees
- moved R66 544.7 mm to (56.5, 90.7), turned to 180 degrees
- moved R67 543.1 mm to (58.4, 92.7), turned to 180 degrees
- moved R68 542.4 mm to (60.1, 90.7), turned to 180 degrees
- moved R70 541.0 mm to (63.8, 90.7), turned to 180 degrees
- moved R69 540.8 mm to (61.9, 92.7), turned to 180 degrees
- moved R71 539.4 mm to (65.6, 92.7), turned to 180 degrees
- moved R72 538.6 mm to (67.5, 90.7), turned to 180 degrees
- moved R114 523.8 mm to (56.8, 109.3), turned to 180 degrees
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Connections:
- C15 pad 1: GND_M90 -> +3.3V_M90
- C15 pad 2: +3.3V_M90 -> GND_M90
- J9 pad 1: /Connectors/Ua -> /Connectors/Uc
- J9 pad 3: /Connectors/Uc -> /Connectors/Ua
- L3 pad 2: GND_M90 -> +3.3V_M90
- U13 pad 7: +3.3V_M90 -> GND_M90
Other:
- board size 13 x 1.4 mm -> 1.4 x 13 mm
